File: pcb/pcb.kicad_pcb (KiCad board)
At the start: 2 copper layers, 120 x 87 mm, 52 parts, among them Q201 IRL540N, T201 DA2032-AL, U1 K155ID1, U2 K155ID1, U201 LM5155, U3 K155ID1, U4 K155ID1

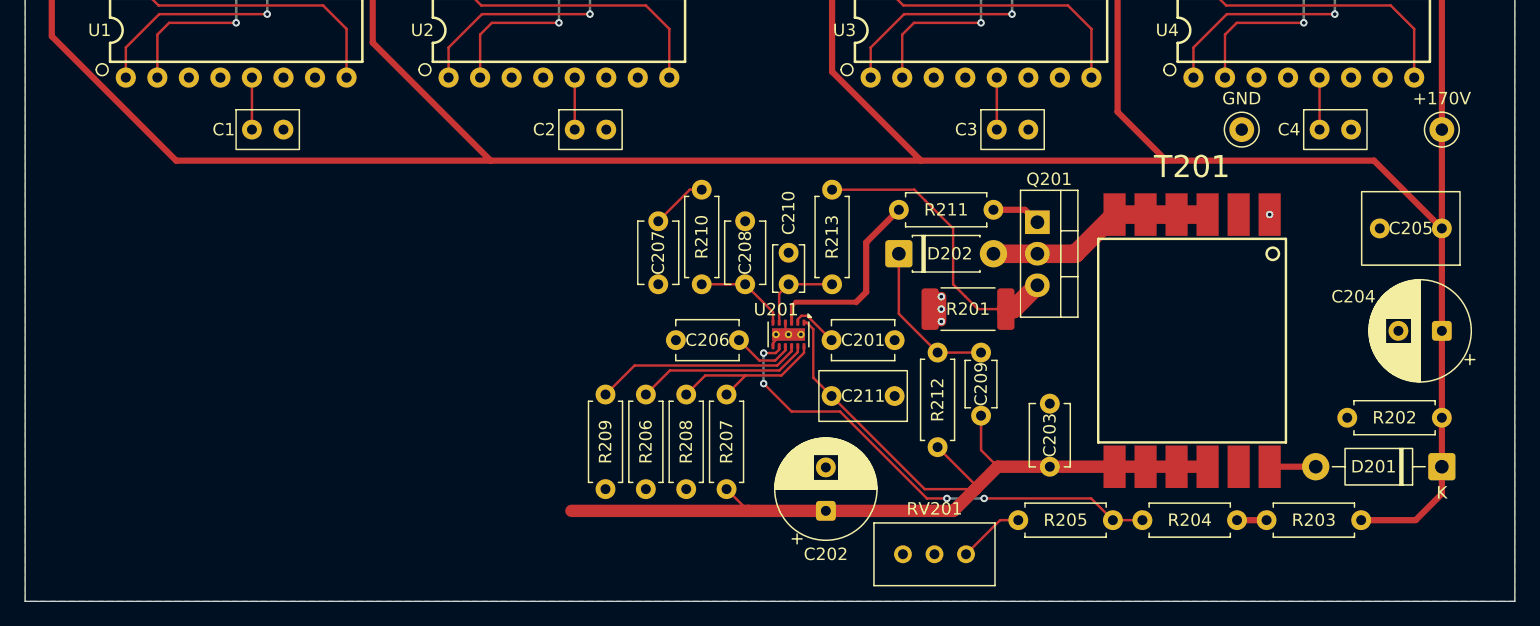
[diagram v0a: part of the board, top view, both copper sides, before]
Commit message: Add USB-PD and 3.3V and 5v converters
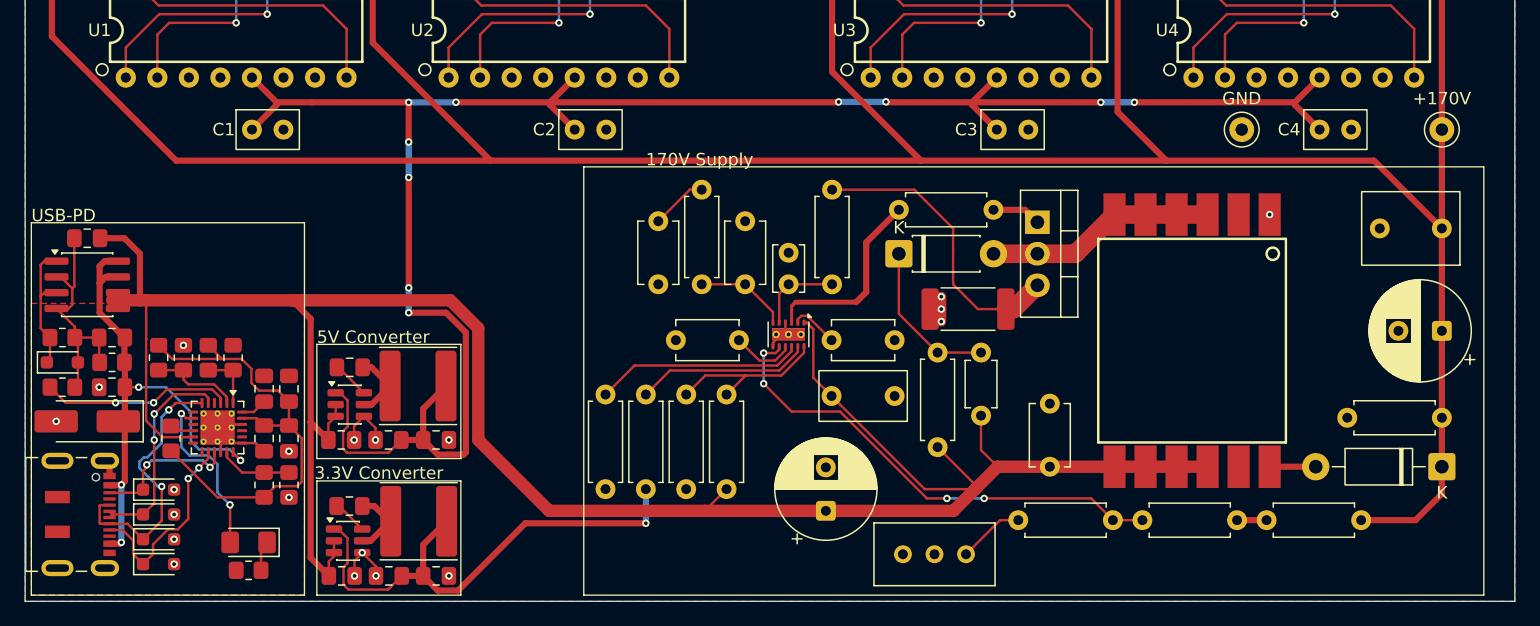
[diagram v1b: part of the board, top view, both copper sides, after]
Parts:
- added C301: 1uF, Capacitor_SMD:C_0805_2012Metric_Pad1.18x1.45mm_HandSolder, F.Cu at (81.2, 108.9)
- added C302: 4.7uF, Capacitor_SMD:C_0805_2012Metric_Pad1.18x1.45mm_HandSolder, F.Cu at (69.0, 108.8)
- added C303: 100nF, Capacitor_SMD:C_0805_2012Metric_Pad1.18x1.45mm_HandSolder, F.Cu at (81.2, 112.9)
- added C304: 100nF, Capacitor_SMD:C_0805_2012Metric_Pad1.18x1.45mm_HandSolder, F.Cu at (83.2, 112.9)
- added C305: 1uF, Capacitor_SMD:C_0805_2012Metric_Pad1.18x1.45mm_HandSolder, F.Cu at (83.2, 108.9)
- added C306: 1uF, Capacitor_SMD:C_0805_2012Metric_Pad1.18x1.45mm_HandSolder, F.Cu at (69.0, 104.8)
- added C307: 1uF, Capacitor_SMD:C_0805_2012Metric_Pad1.18x1.45mm_HandSolder, F.Cu at (67.0, 96.8)
- added C401: 10uF, Capacitor_SMD:C_0805_2012Metric_Pad1.18x1.45mm_HandSolder, F.Cu at (87.5, 113.0)
- added C402: 100nF, Capacitor_SMD:C_0805_2012Metric_Pad1.18x1.45mm_HandSolder, F.Cu at (88.2, 107.2)
- added C403: 22uF, Capacitor_SMD:C_0805_2012Metric_Pad1.18x1.45mm_HandSolder, F.Cu at (91.3, 113.0)
- added C404: 22uF, Capacitor_SMD:C_0805_2012Metric_Pad1.18x1.45mm_HandSolder, F.Cu at (95.1, 113.0)
- added C411: 10uF, Capacitor_SMD:C_0805_2012Metric_Pad1.18x1.45mm_HandSolder, F.Cu at (87.5, 124.0)
- added C412: 100nF, Capacitor_SMD:C_0805_2012Metric_Pad1.18x1.45mm_HandSolder, F.Cu at (88.1, 118.3)
- added C413: 22uF, Capacitor_SMD:C_0805_2012Metric_Pad1.18x1.45mm_HandSolder, F.Cu at (91.3, 124.0)
- added C414: 22uF, Capacitor_SMD:C_0805_2012Metric_Pad1.18x1.45mm_HandSolder, F.Cu at (95.1, 124.0)
- added D301: ESDA051, Diode_SMD:D_SOD-323_HandSoldering, F.Cu at (72.8, 119.0)
- added D302: ESDA051, Diode_SMD:D_SOD-323_HandSoldering, F.Cu at (72.8, 121.0)
- added D303: ESDA051-1JY, Diode_SMD:D_SOD-323_HandSoldering, F.Cu at (72.8, 117.0)
- added D304: ESDA051-1JY, Diode_SMD:D_SOD-323_HandSoldering, F.Cu at (72.8, 123.0)
- added D305: SMAJ15A, Diode_SMD:D_SMA_Handsoldering, F.Cu at (67.0, 111.5)
- added D306: MM3Z10VST1G, Diode_SMD:D_SOD-323_HandSoldering, F.Cu at (65.0, 106.8)
- added D307: LED, LED_SMD:LED_1206_3216Metric_Pad1.42x1.75mm_HandSolder, F.Cu at (80.0, 121.2)
- added J301: USB_C_Receptacle_USB2.0_16P, nixie_clock:USB_C_Receptacle_JAE_DX07S016JA1R1500, F.Cu at (65.8, 119.0)
- added L401: 4.7uH, Inductor_SMD:L_APV_ANR6045, F.Cu at (93.7, 108.7)
- added L411: 4.7uH, Inductor_SMD:L_APV_ANR6045, F.Cu at (93.7, 119.5)
- added Q301: Q_Dual_PMOS_S1G1S2G2D2D2D1D1, Package_SO:SOIC-8_3.9x4.9mm_P1.27mm, F.Cu at (67.0, 100.5)
- added R301: 5.1k, Resistor_SMD:R_0805_2012Metric_Pad1.20x1.40mm_HandSolder, F.Cu at (76.8, 106.4)
- added R302: 1k, Resistor_SMD:R_0805_2012Metric_Pad1.20x1.40mm_HandSolder, F.Cu at (78.8, 106.4)
- added R303: 5.1k, Resistor_SMD:R_0805_2012Metric_Pad1.20x1.40mm_HandSolder, F.Cu at (72.8, 106.4)
- added R304: 2.4k, Resistor_SMD:R_0805_2012Metric_Pad1.20x1.40mm_HandSolder, F.Cu at (74.8, 106.4)
- added R305: 5.1k, Resistor_SMD:R_0805_2012Metric_Pad1.20x1.40mm_HandSolder, F.Cu at (81.2, 116.6)
- added R306: 1k, Resistor_SMD:R_0805_2012Metric_Pad1.20x1.40mm_HandSolder, F.Cu at (83.2, 116.6)
- added R307: 1k, Resistor_SMD:R_0805_2012Metric_Pad1.20x1.40mm_HandSolder, F.Cu at (73.8, 112.9)
- added R308: 10k, Resistor_SMD:R_0805_2012Metric_Pad1.20x1.40mm_HandSolder, F.Cu at (69.0, 106.8)
- added R309: 49.9K, Resistor_SMD:R_0805_2012Metric_Pad1.20x1.40mm_HandSolder, F.Cu at (65.0, 104.8)
- added R310: 1k, Resistor_SMD:R_0805_2012Metric_Pad1.20x1.40mm_HandSolder, F.Cu at (65.0, 108.8)
- added R311: 220, Resistor_SMD:R_0805_2012Metric_Pad1.20x1.40mm_HandSolder, F.Cu at (80.0, 123.5)
- added U301: CYPD3176, nixie_clock:QFN-24-1EP_4x4mm_P0.5mm_EP2.75x2.75mm_ThermalVias, F.Cu at (77.5, 112.0)
- added U401: AP63205WU, Package_TO_SOT_SMD:TSOT-23-6, F.Cu at (88.2, 110.2)
- added U411: AP63203WU, Package_TO_SOT_SMD:TSOT-23-6, F.Cu at (88.0, 121.1)
- T201: value DA2032-AL -> >VALUE
- U201: footprint nixie_clock:WSON-12-1EP_3x2mm_P0.5mm_EP1x2.65_ThermalVias -> Package_SON:WSON-12-1EP_3x2mm_P0.5mm_EP1x2.65_ThermalVias
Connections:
- net /Power Supply/COMP renamed /HV Supply/COMP
- net /Power Supply/CS renamed /HV Supply/CS
- net /Power Supply/FB renamed /HV Supply/FB
- net /Power Supply/GATE renamed /HV Supply/GATE
- net /Power Supply/HV_{DIV} renamed /HV Supply/HV_{DIV}
- net /Power Supply/HV_{SEC} renamed /HV Supply/HV_{SEC}
- net /Power Supply/PGOOD renamed /HV Supply/PGOOD
- net /Power Supply/RT renamed /HV Supply/RT
- net /Power Supply/SS renamed /HV Supply/SS
- net /Power Supply/UVLO renamed /HV Supply/UVLO
- net /Power Supply/VCC renamed /HV Supply/VCC
- net /Power Supply/V_{SW} renamed /HV Supply/V_{SW}
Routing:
- net +5V: track 16.8 -> 158.7 mm, vias 0 -> 10
- net V_{BUS}: track 86.1 -> 191.0 mm
- net /Input Power/VBUS_{C}: track 0.00 -> 42.9 mm, vias 0 -> 4
- net +3V3: track 0.00 -> 41.1 mm, vias 0 -> 1
- net VDDD: track 0.00 -> 38.1 mm
- net /Input Power/D-: track 0.00 -> 22.3 mm, vias 0 -> 2
- net /Input Power/GATE: track 0.00 -> 19.6 mm
- net /Input Power/D+: track 0.00 -> 17.2 mm, vias 0 -> 2
- net /Input Power/CC2: track 0.00 -> 16.1 mm, vias 0 -> 2
- net Net-(U301-VBUS_CTRL): track 0.00 -> 15.4 mm, vias 0 -> 2
- net GND: track 4.85 -> 20.1 mm, vias 4 -> 20
- net /Input Power/FAULT: track 0.00 -> 14.0 mm, vias 0 -> 2
- net /Input Power/CC1: track 0.00 -> 11.8 mm, vias 0 -> 2
- net /Input Power/SOURCE: track 0.00 -> 11.1 mm
- net Net-(U301-VBUS_MAX): track 0.00 -> 7.32 mm
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- added copper zone on F.Cu, net GND
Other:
- board text added: "170V Supply"
- board text added: "3.3V Converter"
- board text added: "5V Converter"
- board text added: "USB-PD"

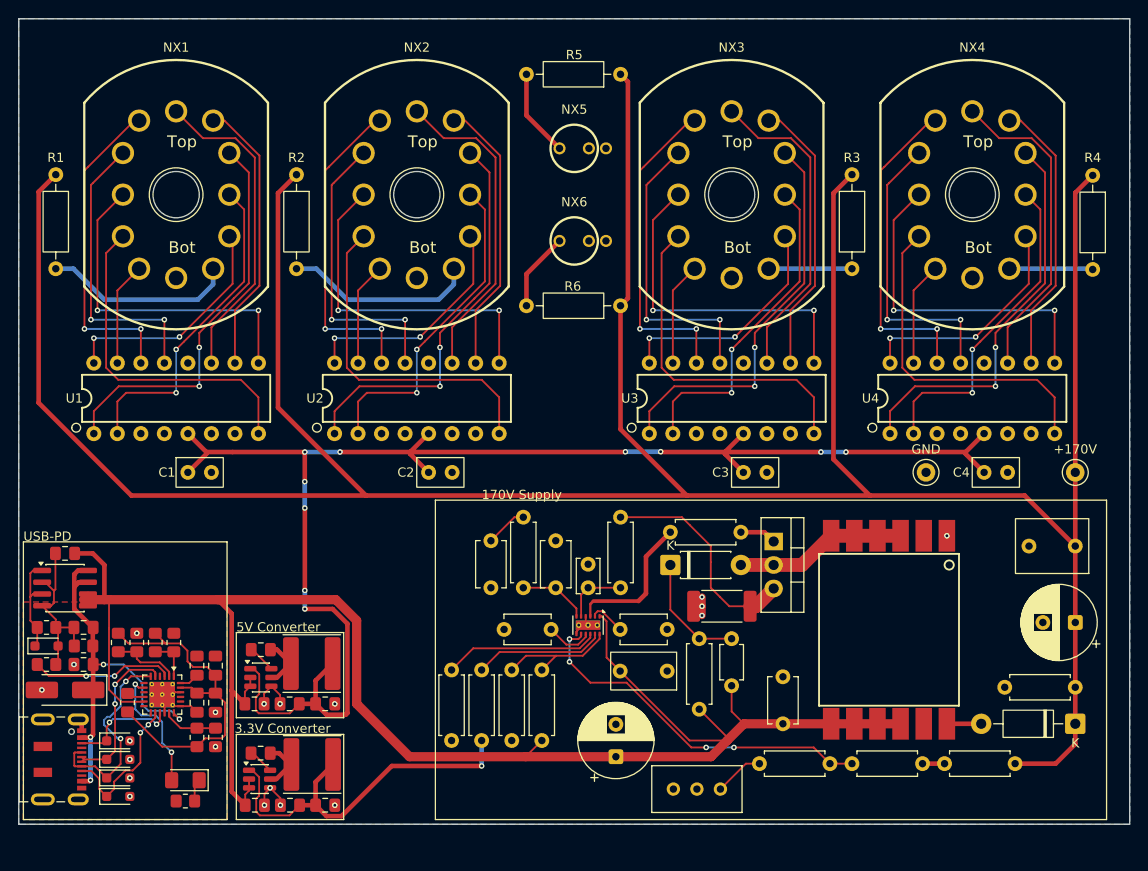
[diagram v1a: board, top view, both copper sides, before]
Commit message: Add title and revision to schematic and board silkscreen, do a bit of tidying of the schematics
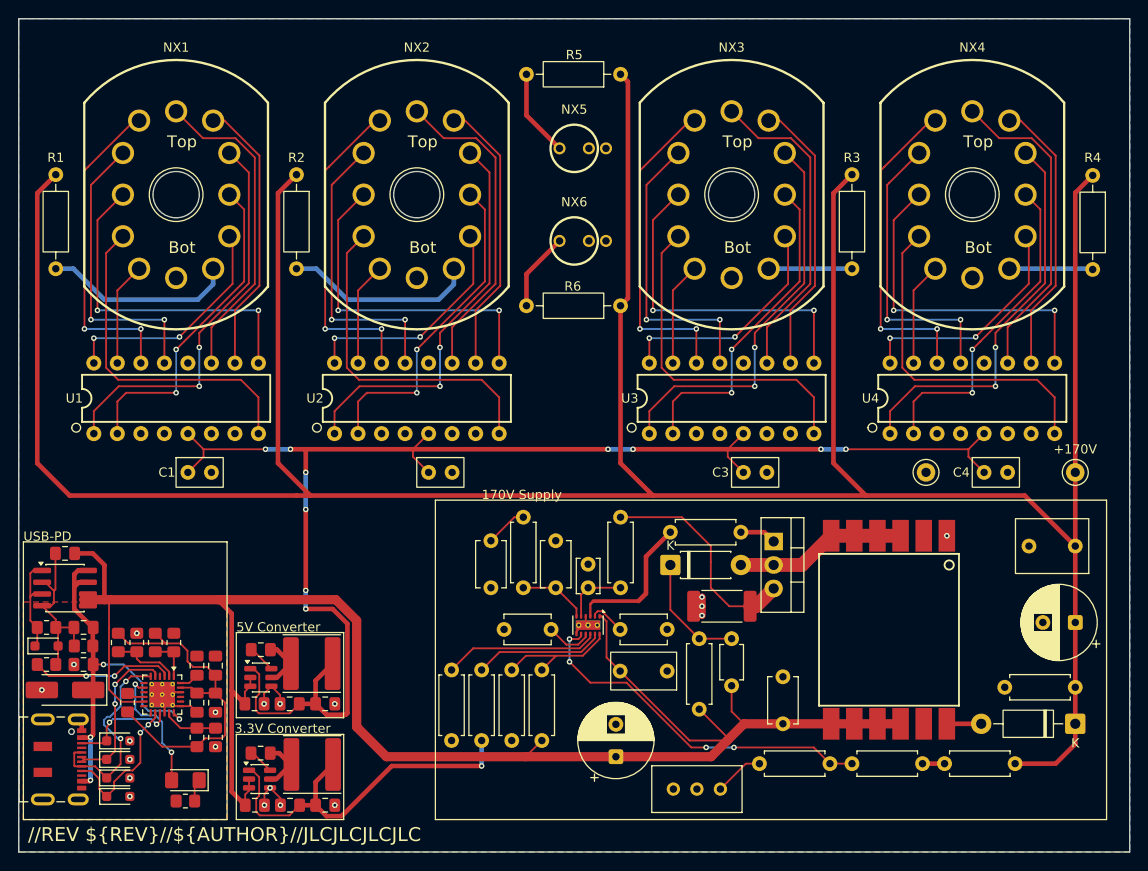
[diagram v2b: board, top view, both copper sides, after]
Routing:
- net V_{BUS}: track 191.0 -> 192.5 mm
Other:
- board size 120 x 87 mm -> 120 x 90 mm
- board text added: "${TITLE}//REV ${REV}//${AUTHOR}//JLCJLCJLCJLC"

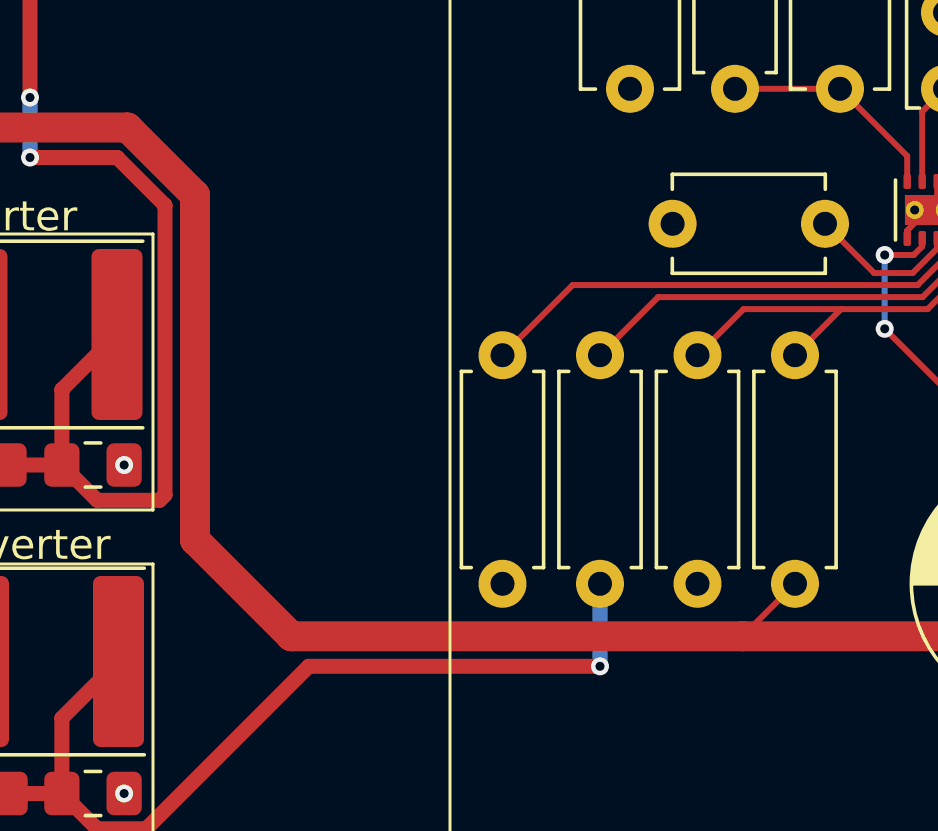
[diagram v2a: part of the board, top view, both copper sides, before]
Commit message: Add readme, license, fix psu_design. move datasheets readme to tube_notes
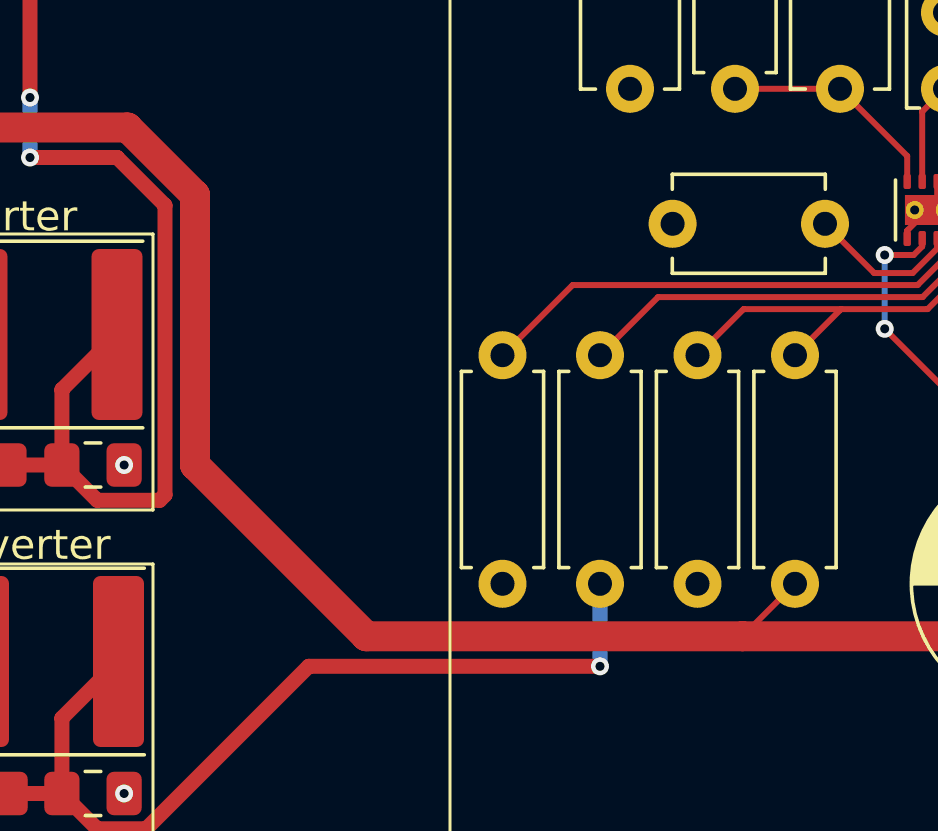
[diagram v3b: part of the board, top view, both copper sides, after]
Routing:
- net V_{BUS}: track 192.5 -> 191.0 mm
